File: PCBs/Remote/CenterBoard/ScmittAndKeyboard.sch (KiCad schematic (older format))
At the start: 4 parts, among them J701 Conn_02x10_Odd_Even, U701 74HC14, U702 74HC14, U703 74HC14

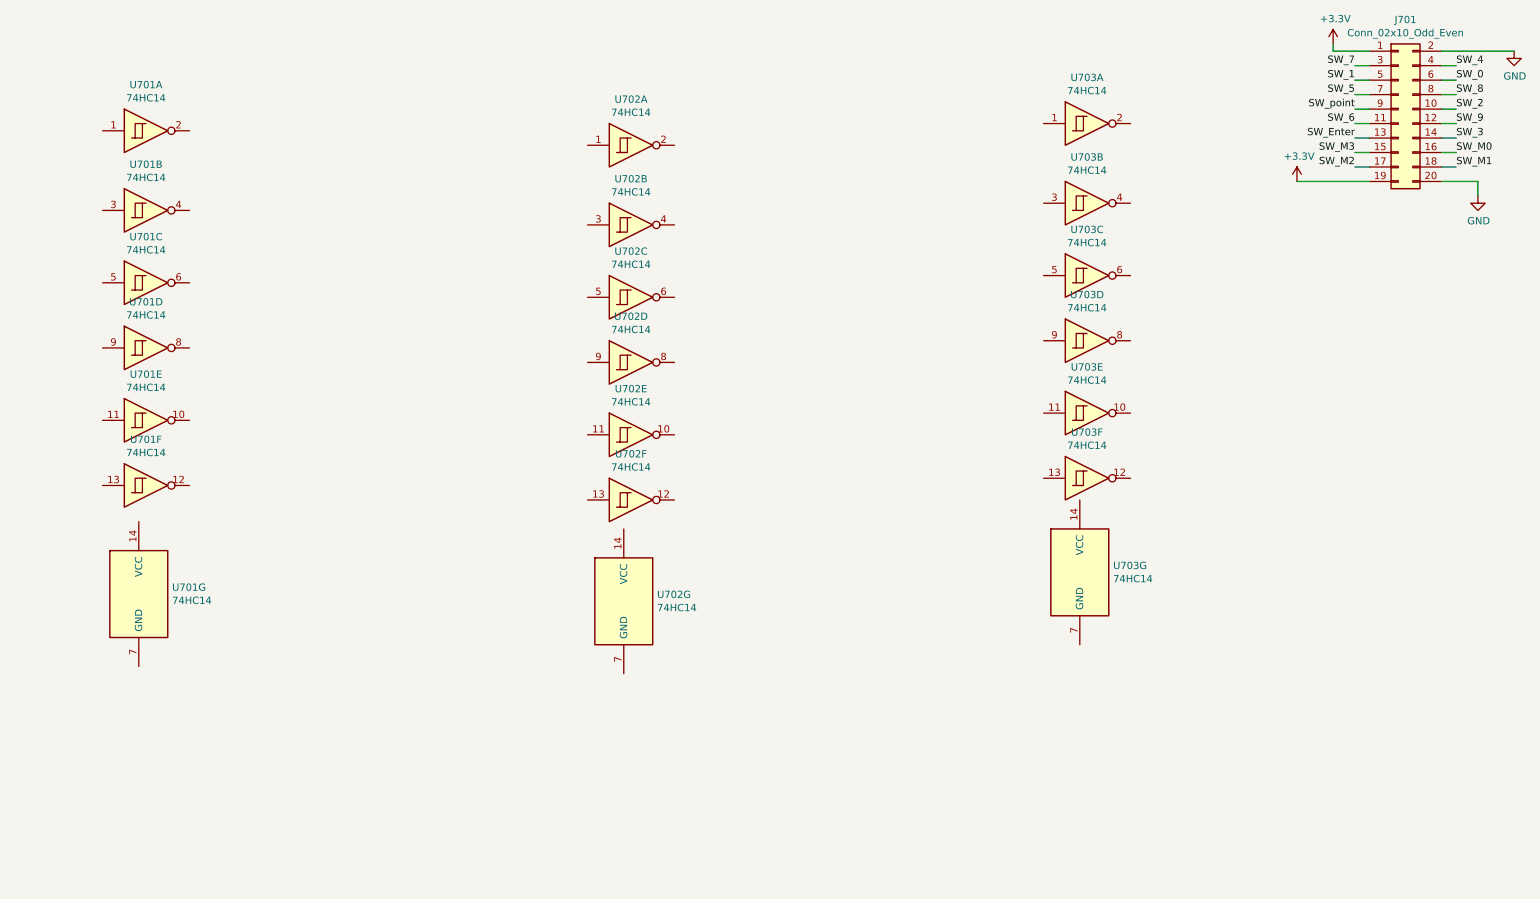
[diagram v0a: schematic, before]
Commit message: Screen POT->PWM and RGB LEDS reworked, making space on the CPU pins. Almost done
Signed-off-by: Eldalote.Electronics <Eldalote.Electronics@gmail.com>
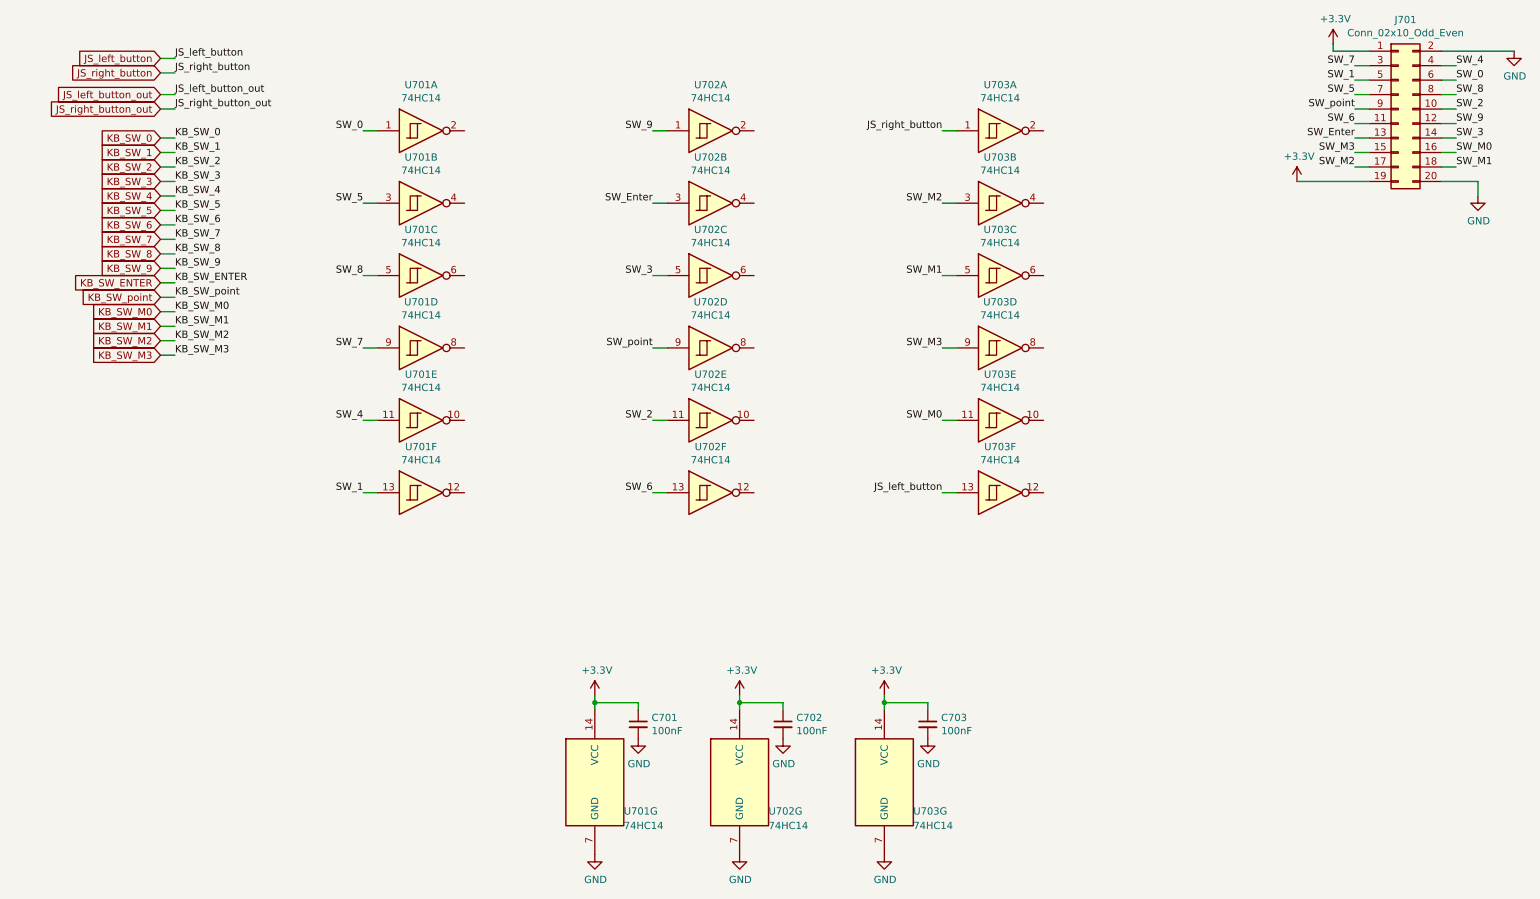
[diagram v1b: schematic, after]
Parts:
- added C701, C702, C703: 100nF, Capacitor_SMD:C_0402_1005Metric, symbol Device:C_Small
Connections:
- net +3V3: now also U701.14 (VCC), U702.14 (VCC), U703.14 (VCC), C701.1, C702.1, C703.1
- net GND: now also U701.7 (GND), U702.7 (GND), U703.7 (GND), C701.2, C702.2, C703.2
- net SW_0: now also U701.1
- net SW_1: now also U701.13
- net SW_2: now also U702.11
- net SW_3: now also U702.5
- net SW_4: now also U701.11
- net SW_5: now also U701.3
- net SW_6: now also U702.13
- net SW_7: now also U701.9
- net SW_8: now also U701.5
- net SW_9: now also U702.1
- net SW_Enter: now also U702.3
- net SW_M0: now also U703.11
- net SW_M1: now also U703.5
- net SW_M2: now also U703.3
- net SW_M3: now also U703.9
- net SW_point: now also U702.9
- net JS_right_button: now reaches U703.1
- net JS_left_button: now reaches U703.13
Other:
- moved on the sheet: U701A, U701B, U701C, U701D, U701E, U701F, U701G, U702A, U702B, U702C, U702D, U702E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

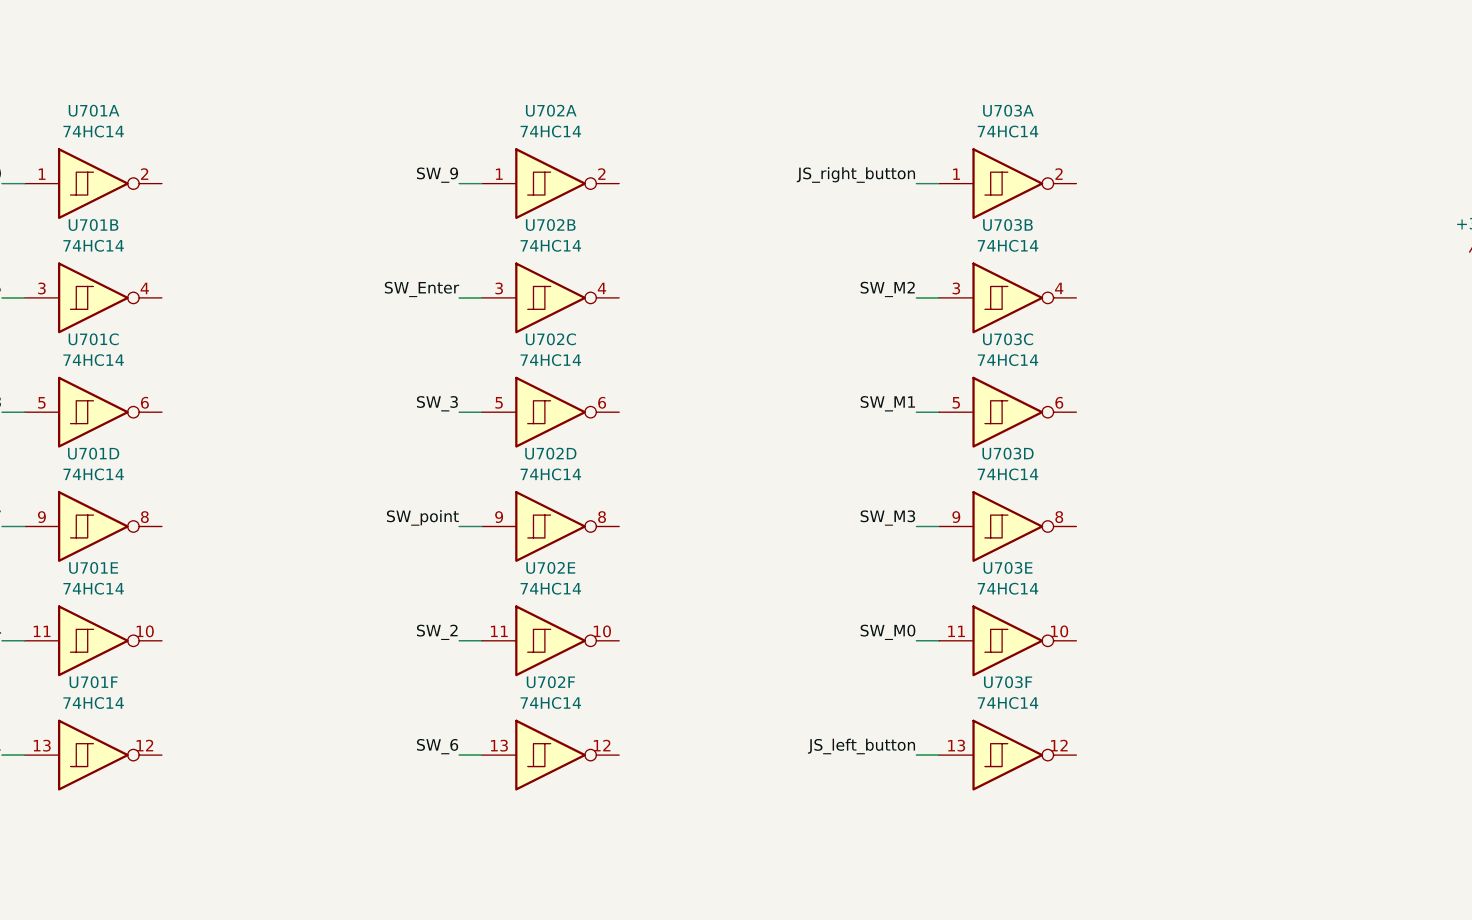
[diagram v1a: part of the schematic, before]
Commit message: Finished leds, redid a lot of PCB wiring. Almost done there now.
Signed-off-by: Eldalote.Electronics <Eldalote.Electronics@gmail.com>
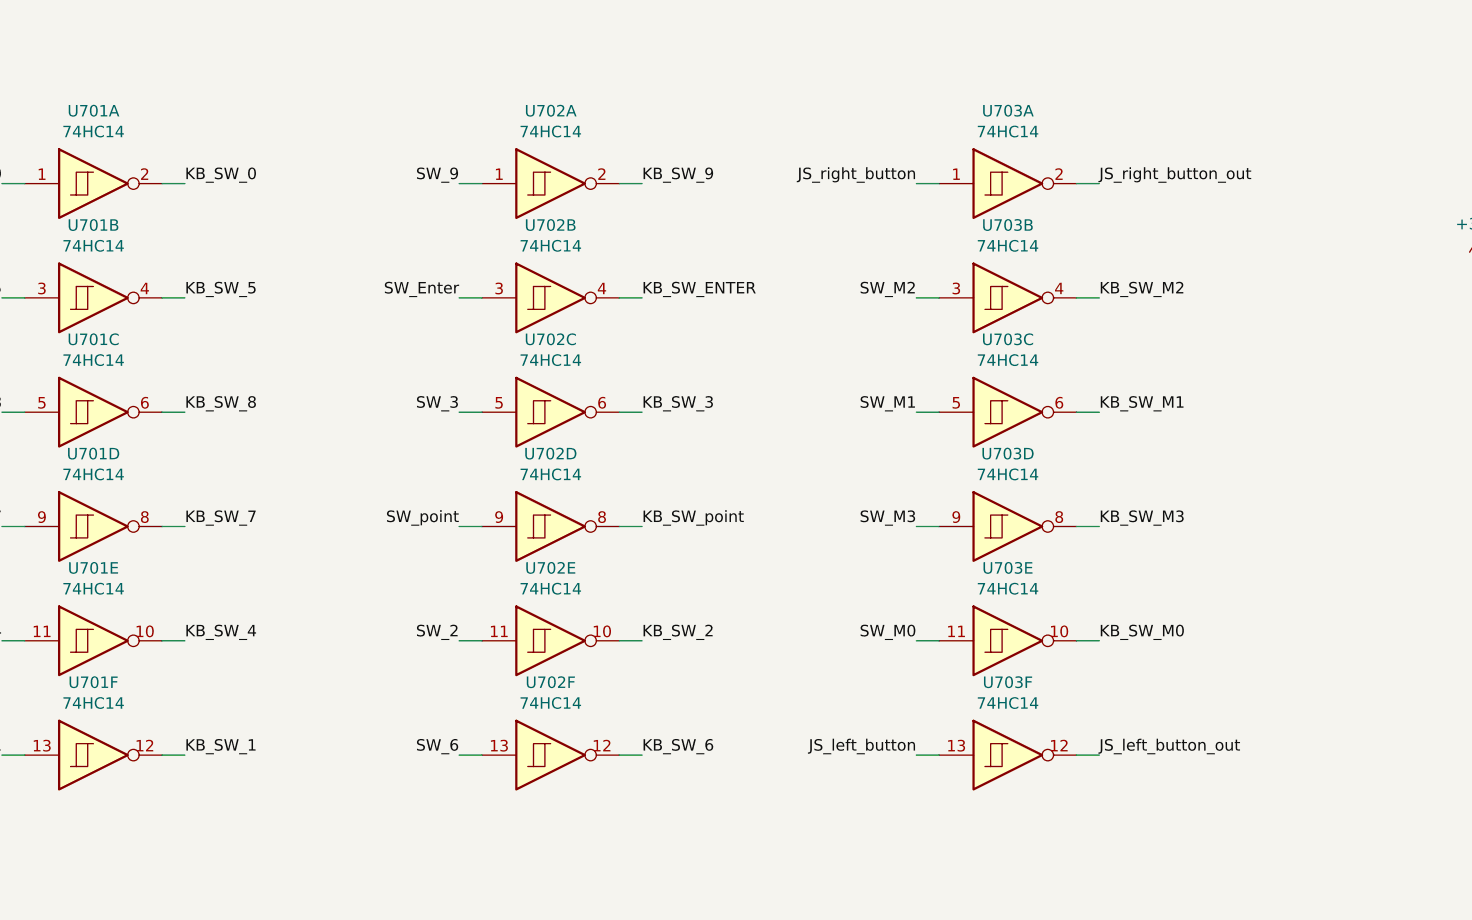
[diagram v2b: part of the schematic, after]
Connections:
- net JS_left_button_out: now also U703.12
- net JS_right_button_out: now also U703.2
- net KB_SW_0: now also U701.2
- net KB_SW_1: now also U701.12
- net KB_SW_2: now also U702.10
- net KB_SW_3: now also U702.6
- net KB_SW_4: now also U701.10
- net KB_SW_5: now also U701.4
- net KB_SW_6: now also U702.12
- net KB_SW_7: now also U701.8
- net KB_SW_8: now also U701.6
- net KB_SW_9: now also U702.2
- net KB_SW_ENTER: now also U702.4
- net KB_SW_M0: now also U703.10
- net KB_SW_M1: now also U703.6
- net KB_SW_M2: now also U703.4
- net KB_SW_M3: now also U703.8
- net KB_SW_point: now also U702.8
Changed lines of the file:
@@
 Text Label 1600 3050 0    50   ~ 0
 KB_SW_M3
+Wire Wire Line
+	3600 1500 3700 1500
+Wire Wire Line
+	3600 4000 3700 4000
+Wire Wire Line
+	5600 3500 5700 3500
+Wire Wire Line
+	5600 2500 5700 2500
+Wire Wire Line
+	3600 3500 3700 3500
+Wire Wire Line
+	5600 4000 5700 4000
+Wire Wire Line
+	3600 3000 3700 3000
+Wire Wire Line
+	3600 2500 3700 2500
+Wire Wire Line
+	5600 1500 5700 1500
+Wire Wire Line
+	5600 2000 5700 2000
+Wire Wire Line
+	5600 3000 5700 3000
+Wire Wire Line
+	7600 3500 7700 3500
+Wire Wire Line
+	7600 2500 7700 2500
+Wire Wire Line
+	7600 2000 7700 2000
+Wire Wire Line
+	7600 3000 7700 3000
+Text Label 3700 1500 0    50   ~ 0
+KB_SW_0
+Text Label 3700 4000 0    50   ~ 0
+KB_SW_1
+Text Label 5700 3500 0    50   ~ 0
+KB_SW_2
+Text Label 5700 2500 0    50   ~ 0
+KB_SW_3
+Text Label 3700 3500 0    50   ~ 0
+KB_SW_4
+Text Label 3700 3000 0    50   ~ 0
+KB_SW_7
+Text Label 3700 2500 0    50   ~ 0
+KB_SW_8
+Text Label 5700 1500 0    50   ~ 0
+KB_SW_9
+Text Label 5700 2000 0    50   ~ 0
+KB_SW_ENTER
+Text Label 5700 3000 0    50   ~ 0
+KB_SW_point
+Text Label 7700 3500 0    50   ~ 0
+KB_SW_M0
+Text Label 7700 2500 0    50   ~ 0
+KB_SW_M1
+Text Label 7700 2000 0    50   ~ 0
+KB_SW_M2
+Text Label 7700 3000 0    50   ~ 0
+KB_SW_M3
+Text Label 5700 4000 0    50   ~ 0
+KB_SW_6
+Text Label 3700 2000 0    50   ~ 0
+KB_SW_5
+Wire Wire Line
+	3600 2000 3700 2000
+Wire Wire Line
+	7600 4000 7700 4000
+Text Label 7700 4000 0    50   ~ 0
+JS_left_button_out
+Wire Wire Line
+	7600 1500 7700 1500
+Text Label 7700 1500 0    50   ~ 0
+JS_right_button_out
 $EndSCHEMATC

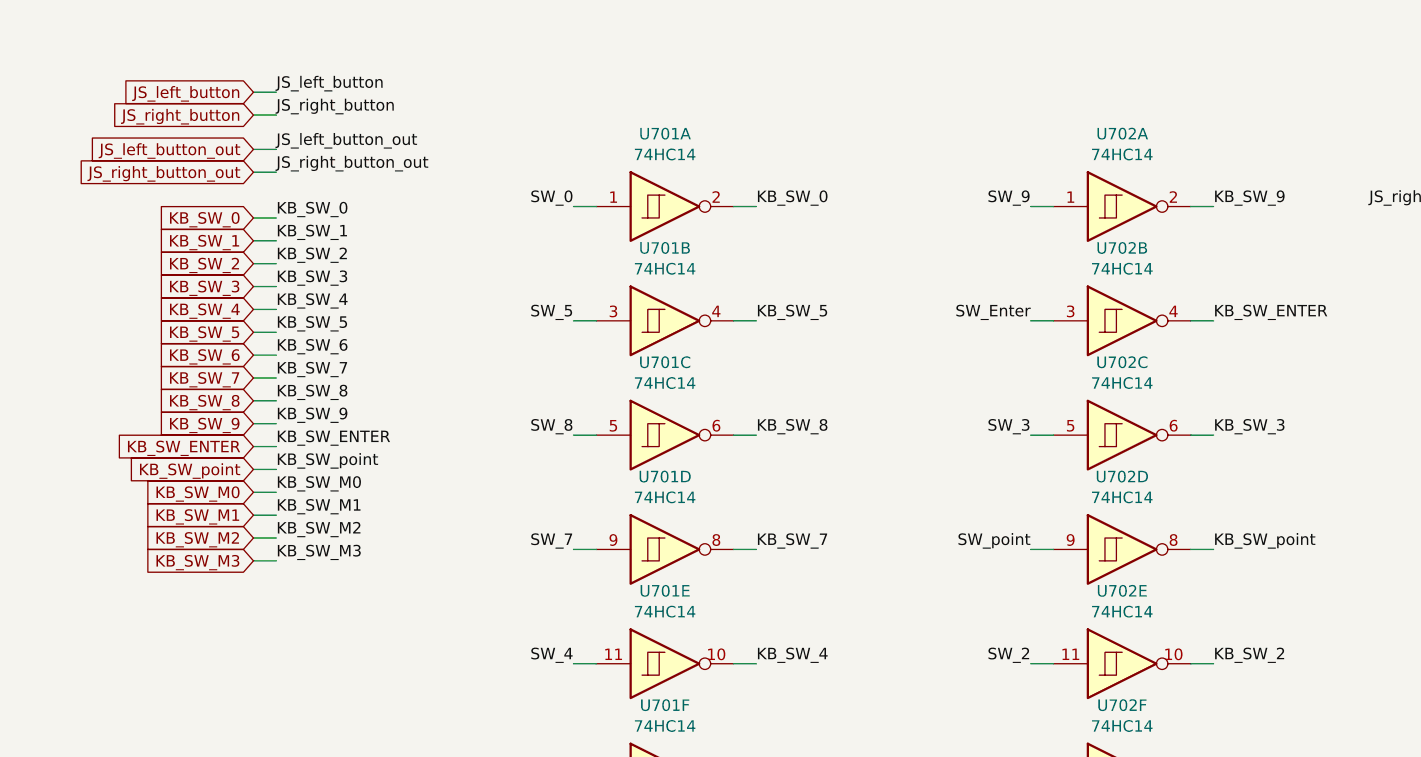
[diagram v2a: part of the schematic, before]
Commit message: More finishing work on remote-centerboard. Copied in the Drone main board, did some cleaning up on that. Started work on  more neat and clean lessons learned documents
Signed-off-by: Eldalote.Electronics <Eldalote.Electronics@gmail.com>
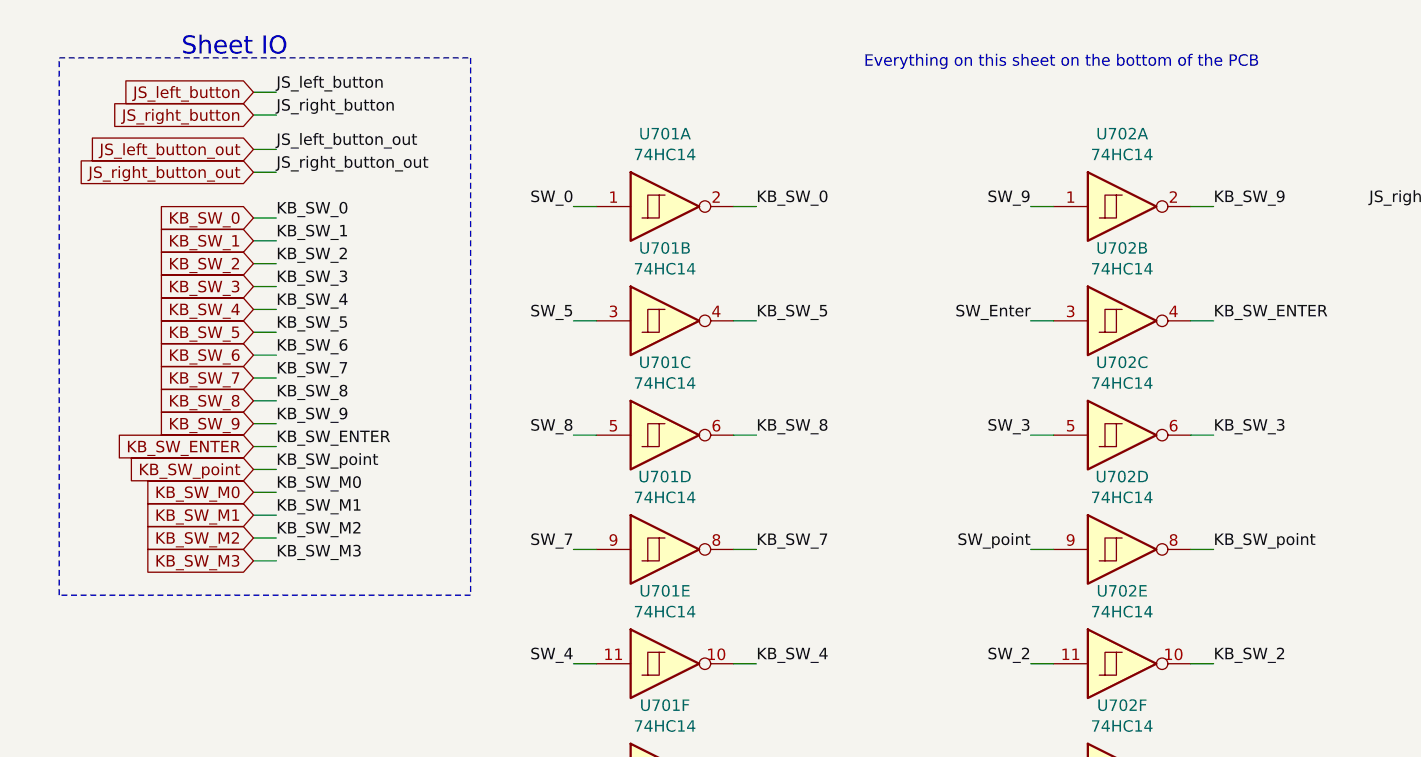
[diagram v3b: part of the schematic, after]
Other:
- note added: "Everything on this sheet on the bottom of the PCB"
- note added: "Sheet IO"
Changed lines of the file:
@@
 Text Label 7700 1500 0    50   ~ 0
 JS_right_button_out
+Wire Notes Line
+	2450 850  2450 3200
+Wire Notes Line
+	2450 3200 650  3200
+Wire Notes Line
+	650  3200 650  850
+Wire Notes Line
+	650  850  2450 850
+Text Notes 1650 850  2    79   ~ 0
+Sheet IO
+Text Notes 5900 900  2    50   ~ 0
+Everything on this sheet on the bottom of the PCB
 $EndSCHEMATC
